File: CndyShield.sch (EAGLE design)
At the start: 19 parts, among them U1 ARDUINOR3-BPLACE

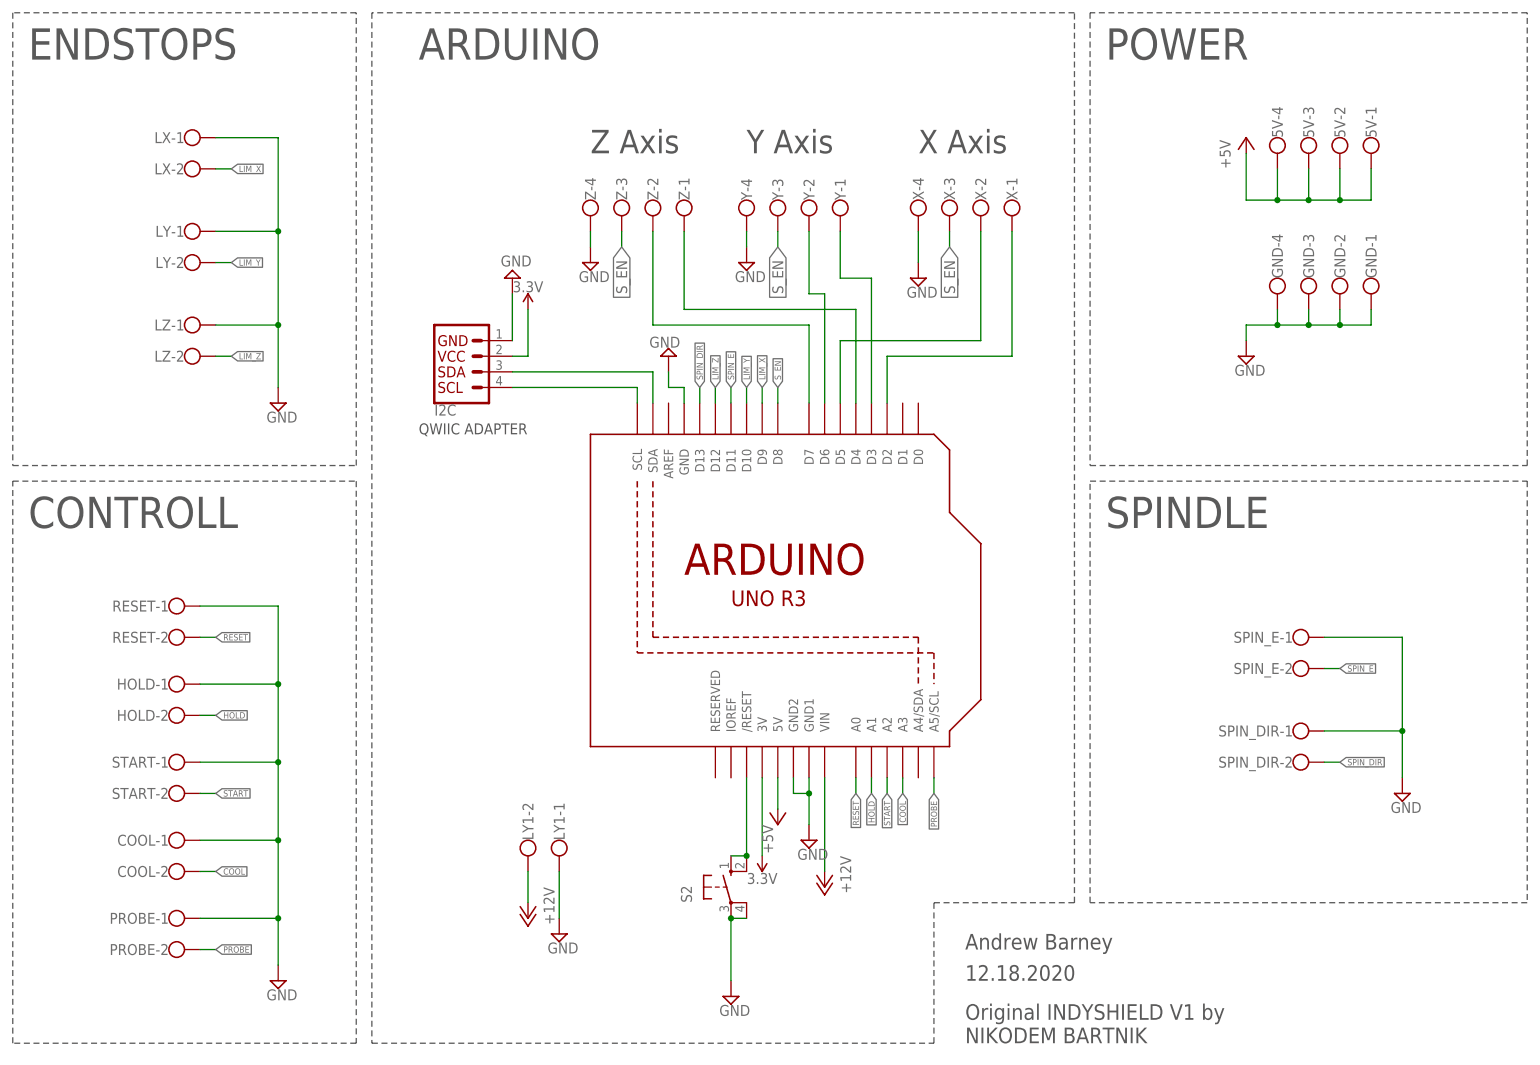
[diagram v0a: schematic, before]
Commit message: Add files via upload
V1.1 : remapped analog breakouts. Added filter capacitors. Added Alarm State LED on A4.
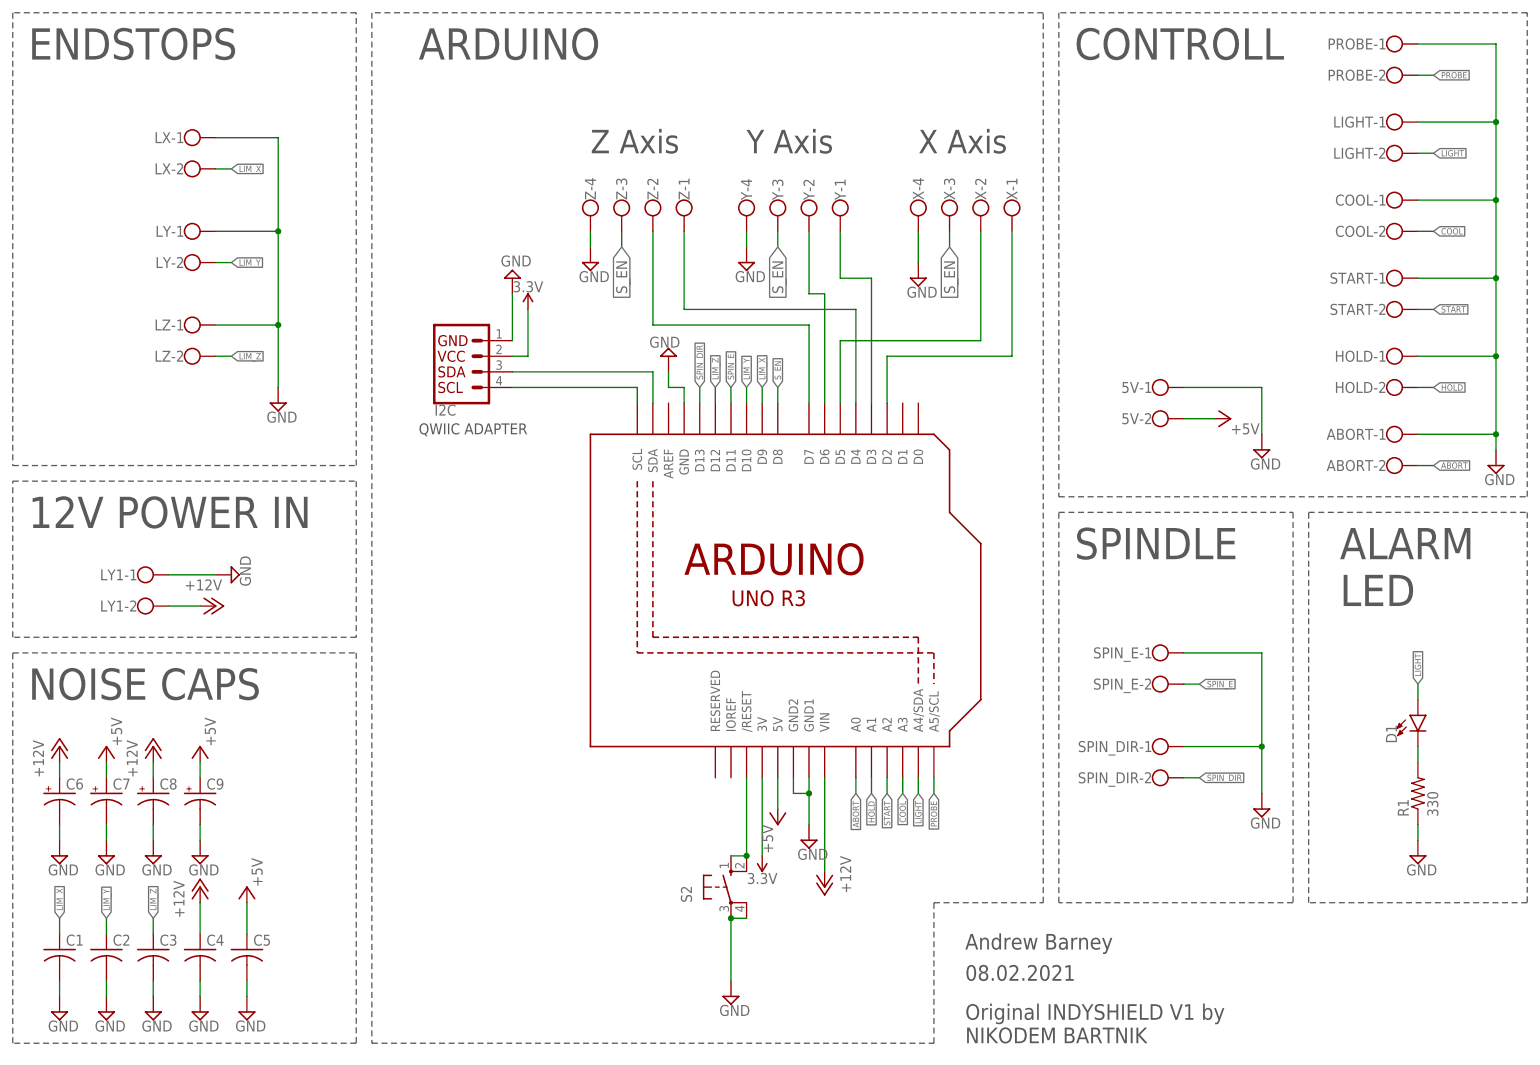
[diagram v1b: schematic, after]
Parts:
- removed GND: (no value), con-wago-500:W237-4
- removed RESET: (no value), con-wago-500:W237-102
- added ABORT, LIGHT: (no value), con-wago-500:W237-102
- added C1, C2, C3, C4, C5: (no value), adafruit:C-US025-024X044
- added C6, C7, C8, C9: (no value), adafruit:CPOL-USE1.8-4
- added D1: (no value), SparkFun-LED:LED5MM
- added R1: 330, adafruit:R-US_0207/10
- 5V: device con-wago-500:W237-4 -> con-wago-500:W237-102
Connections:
- removed net RESET: RESET-2.KL, U1.A0
- new net ABORT: ABORT-2.KL, U1.A0
- new net LIGHT: D1.A, LIGHT-2.KL, U1.A4/SDA
- new net N$8: D1.C, R1.2
- net +12V: now also C4.1, C6.+, C8.+
- net +5V: now also C5.1, C7.+, C9.+; no longer 5V-1.KL, 5V-3.KL, 5V-4.KL
- net GND: now also 5V-1.KL, ABORT-1.KL, C1.2, C2.2, C3.2, C4.2, C5.2, C6.-, C7.-, C8.-, C9.-, LIGHT-1.KL, R1.1; no longer GND-1.KL, GND-2.KL, GND-3.KL, GND-4.KL, RESET-1.KL
- net LIM_X: now also C1.1
- net LIM_Y: now also C2.1
- net LIM_Z: now also C3.1
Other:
- note added: "08.02.2021"
- note added: "12V POWER IN"
- note added: "ALARM LED"
- note added: "NOISE CAPS"
- note removed: "12.18.2020"
- note removed: "POWER"
- moved on the sheet: 5V-1, 5V-2, COOL-1, COOL-2, HOLD-1, HOLD-2, LY1-1, LY1-2, PROBE-1, PROBE-2, SPIN_DIR-1, SPIN_DIR-2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

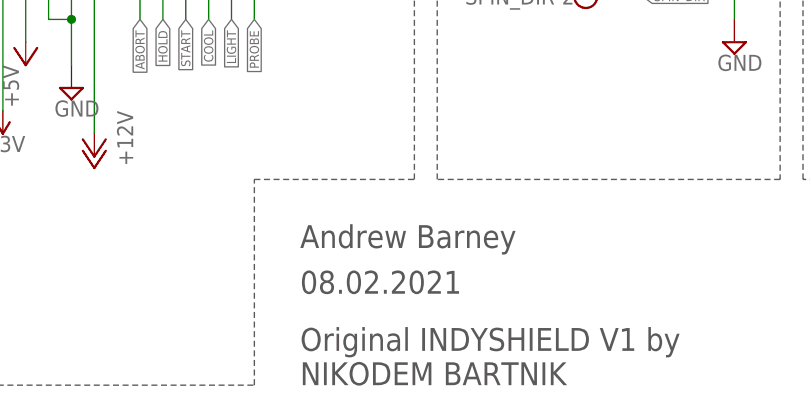
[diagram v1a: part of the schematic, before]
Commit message: Add files via upload
minor silkscreen change for Analog 4. Changed LIGHT to MIST to be more consistent with official GRBL port use.
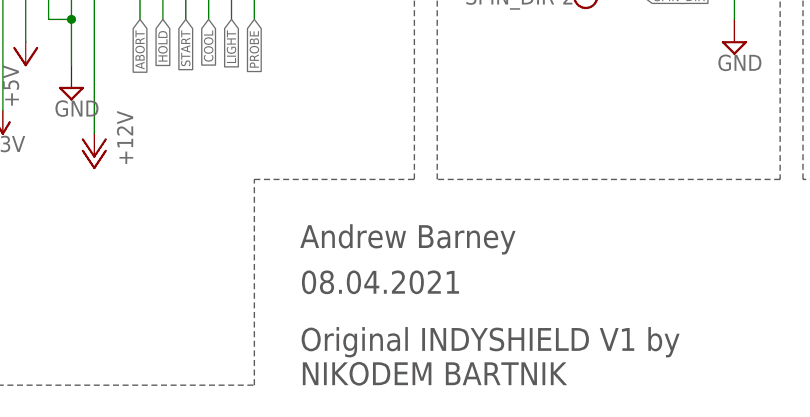
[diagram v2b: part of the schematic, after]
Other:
- note added: "08.04.2021"
- note removed: "08.02.2021"
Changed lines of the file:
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@@
 <text x="10.16" y="88.9" size="5.08" layer="97">12V POWER IN</text>
 <text x="162.56" y="20.32" size="2.54" layer="97">Andrew Barney</text>
-<text x="162.56" y="15.24" size="2.54" layer="97">08.02.2021</text>
+<text x="162.56" y="15.24" size="2.54" layer="97">08.04.2021</text>
 <text x="73.66" y="104.14" size="1.778" layer="97">QWIIC ADAPTER</text>
 <text x="162.56" y="5.08" size="2.54" layer="97">Original INDYSHIELD V1 by

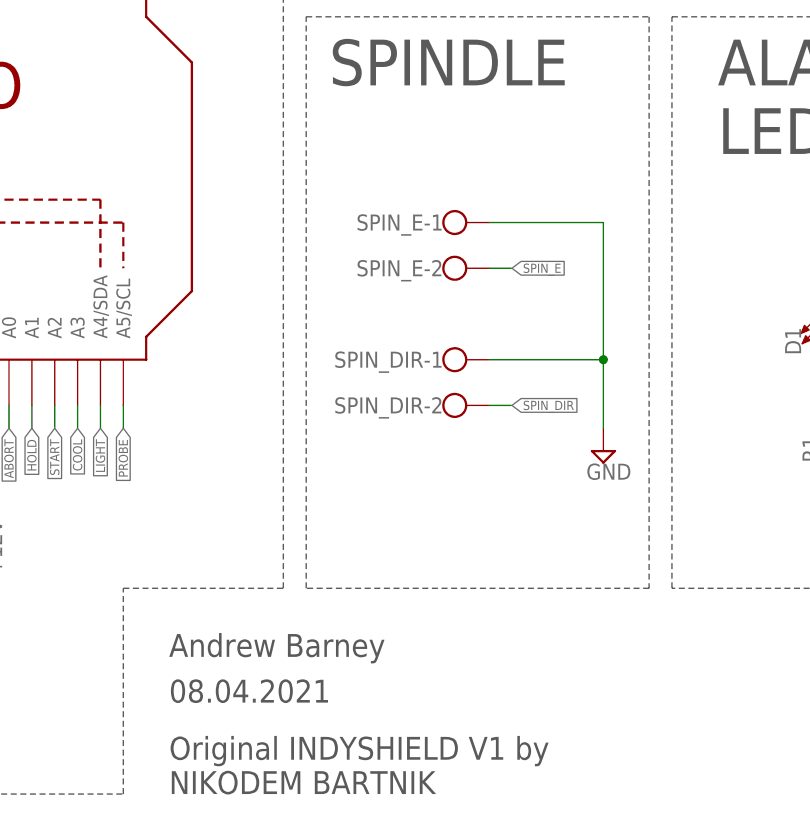
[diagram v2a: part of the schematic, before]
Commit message: Add files via upload
V1.2: Fixed swapped silkscreen text for Spindle PWM and Spindle Direction. Added optional LED to Spindle PWM (pin 11) as an optional safety warning light.
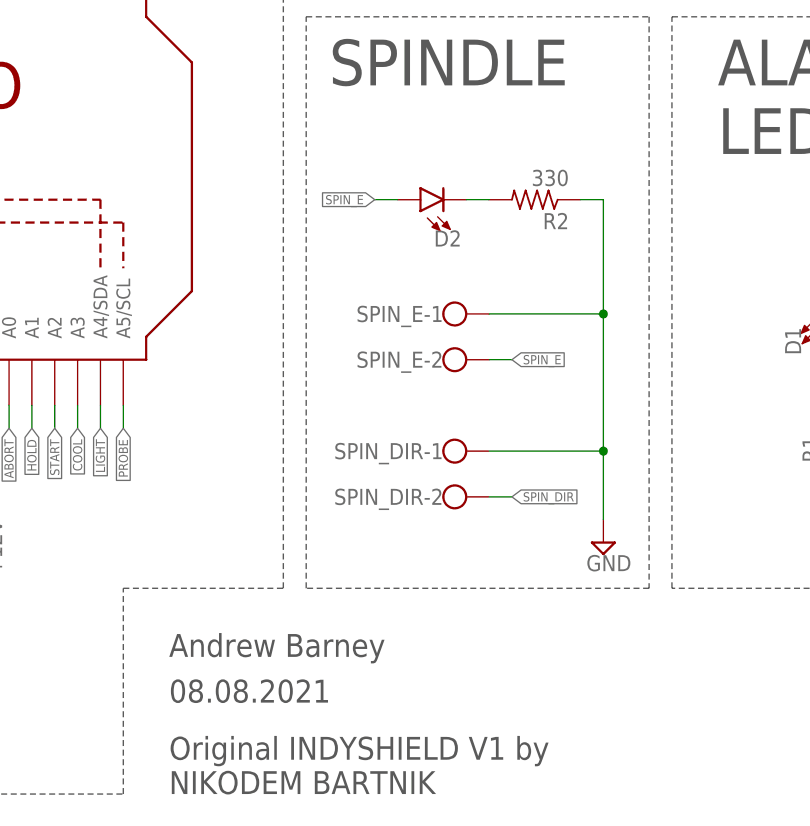
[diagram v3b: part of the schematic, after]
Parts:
- added D2: (no value), SparkFun-LED:LED5MM
- added R2: 330, adafruit:R-US_0207/10
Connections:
- new net N$11: D2.C, R2.2
- net GND: now also R2.1
- net SPIN_E: now also D2.A
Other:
- note added: "08.08.2021"
- note removed: "08.04.2021"
- moved on the sheet: SPIN_DIR-1, SPIN_DIR-2, SPIN_E-1, SPIN_E-2
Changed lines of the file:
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@@
 <part name="P+9" library="supply1" library_urn="urn:adsk.eagle:library:371" deviceset="+12V" device=""/>
 <part name="P+10" library="supply1" library_urn="urn:adsk.eagle:library:371" deviceset="+5V" device=""/>
+<part name="D2" library="SparkFun-LED" library_urn="urn:adsk.eagle:library:529" deviceset="LED" device="5MM" package3d_urn="urn:adsk.eagle:package:39353/1"/>
+<part name="R2" library="adafruit" library_urn="urn:adsk.eagle:library:420" deviceset="R-US_" device="0207/10" package3d_urn="urn:adsk.eagle:package:6240597/1" value="330"/>
 </parts>
 <sheets>
@@
 <text x="10.16" y="88.9" size="5.08" layer="97">12V POWER IN</text>
 <text x="162.56" y="20.32" size="2.54" layer="97">Andrew Barney</text>
-<text x="162.56" y="15.24" size="2.54" layer="97">08.04.2021</text>
+<text x="162.56" y="15.24" size="2.54" layer="97">08.08.2021</text>
 <text x="73.66" y="104.14" size="1.778" layer="97">QWIIC ADAPTER</text>
 <text x="162.56" y="5.08" size="2.54" layer="97">Original INDYSHIELD V1 by
@@
 <attribute name="VALUE" x="48.895" y="106.045" size="1.778" layer="96"/>
 </instance>
-<instance part="SPIN_E" gate="-1" x="193.04" y="68.58" smashed="yes">
-<attribute name="NAME" x="193.04" y="69.469" size="1.778" layer="95" rot="R180"/>
-</instance>
-<instance part="SPIN_E" gate="-2" x="193.04" y="63.5" smashed="yes">
-<attribute name="VALUE" x="190.5" y="59.817" size="1.778" layer="96"/>
-<attribute name="NAME" x="193.04" y="64.389" size="1.778" layer="95" rot="R180"/>
-</instance>
-<instance part="SPIN_DIR" gate="-1" x="193.04" y="53.34" smashed="yes">
+<instance part="SPIN_E" gate="-1" x="193.04" y="58.42" smashed="yes">
+<attribute name="NAME" x="193.04" y="59.309" size="1.778" layer="95" rot="R180"/>
+</instance>
+<instance part="SPIN_E" gate="-2" x="193.04" y="53.34" smashed="yes">
+<attribute name="VALUE" x="190.5" y="49.657" size="1.778" layer="96"/>
 <attribute name="NAME" x="193.04" y="54.229" size="1.778" layer="95" rot="R180"/>
 </instance>
-<instance part="SPIN_DIR" gate="-2" x="193.04" y="48.26" smashed="yes">
-<attribute name="VALUE" x="190.5" y="44.577" size="1.778" layer="96"/>
-<attribute name="NAME" x="193.04" y="49.149" size="1.778" layer="95" rot="R180"/>
-</instance>
-<instance part="SUPPLY6" gate="GND" x="210.82" y="43.18" smashed="yes">
-<attribute name="VALUE" x="208.915" y="40.005" size="1.778" layer="96"/>
+<instance part="SPIN_DIR" gate="-1" x="193.04" y="43.18" smashed="yes">
+<attribute name="NAME" x="193.04" y="44.069" size="1.778" layer="95" rot="R180"/>
+</instance>
+<instance part="SPIN_DIR" gate="-2" x="193.04" y="38.1" smashed="yes">
+<attribute name="VALUE" x="190.5" y="34.417" size="1.778" layer="96"/>
+<attribute name="NAME" x="193.04" y="38.989" size="1.778" layer="95" rot="R180"/>
+</instance>
+<instance part="SUPPLY6" gate="GND" x="210.82" y="33.02" smashed="yes">
+<attribute name="VALUE" x="208.915" y="29.845" size="1.778" layer="96"/>
 </instance>
 <instance part="SUPPLY7" gate="GND" x="114.3" y="116.84" smashed="yes" rot="R180">
@@
 <instance part="P+10" gate="1" x="38.1" y="53.34" smashed="yes">
 <attribute name="VALUE" x="40.64" y="53.34" size="1.778" layer="96" rot="R90"/>
+</instance>
+<instance part="D2" gate="G$1" x="190.5" y="71.12" smashed="yes" rot="R90">
+<attribute name="NAME" x="195.072" y="67.691" size="1.778" layer="95" font="vector" rot="R180"/>
+<attribute name="VALUE" x="195.072" y="73.025" size="1.778" layer="96" font="vector" rot="R180" align="top-left"/>
+</instance>
+<instance part="R2" gate="G$1" x="203.2" y="71.12" smashed="yes" rot="R180">
+<attribute name="NAME" x="207.01" y="69.6214" size="1.778" layer="95" rot="R180"/>
+<attribute name="VALUE" x="207.01" y="74.422" size="1.778" layer="96" rot="R180"/>
 </instance>
 </instances>
@@
 <pinref part="SPIN_E" gate="-1" pin="KL"/>
 <pinref part="SUPPLY6" gate="GND" pin="GND"/>
-<wire x1="198.12" y1="68.58" x2="210.82" y2="68.58" width="0.1524" layer="91"/>
-<wire x1="210.82" y1="68.58" x2="210.82" y2="53.34" width="0.1524" layer="91"/>
+<wire x1="198.12" y1="58.42" x2="210.82" y2="58.42" width="0.1524" layer="91"/>
+<wire x1="210.82" y1="58.42" x2="210.82" y2="43.18" width="0.1524" layer="91"/>
 <pinref part="SPIN_DIR" gate="-1" pin="KL"/>
-<wire x1="210.82" y1="53.34" x2="210.82" y2="45.72" width="0.1524" layer="91"/>
-<wire x1="198.12" y1="53.34" x2="210.82" y2="53.34" width="0.1524" layer="91"/>
-<junction x="210.82" y="53.34"/>
+<wire x1="210.82" y1="43.18" x2="210.82" y2="35.56" width="0.1524" layer="91"/>
+<wire x1="198.12" y1="43.18" x2="210.82" y2="43.18" width="0.1524" layer="91"/>
+<junction x="210.82" y="43.18"/>
+<pinref part="R2" gate="G$1" pin="1"/>
+<wire x1="208.28" y1="71.12" x2="210.82" y2="71.12" width="0.1524" layer="91"/>
+<wire x1="210.82" y1="71.12" x2="210.82" y2="58.42" width="0.1524" layer="91"/>
+<junction x="210.82" y="58.42"/>
 </segment>
 <segment>
@@
 <segment>
 <pinref part="SPIN_E" gate="-2" pin="KL"/>
-<wire x1="198.12" y1="63.5" x2="200.66" y2="63.5" width="0.1524" layer="91"/>
-<label x="200.66" y="63.5" size="1.016" layer="95" xref="yes"/>
+<wire x1="198.12" y1="53.34" x2="200.66" y2="53.34" width="0.1524" layer="91"/>
+<label x="200.66" y="53.34" size="1.016" layer="95" xref="yes"/>
+<label x="185.42" y="71.12" size="1.016" layer="95" rot="R180" xref="yes"/>
 </segment>
 <segment>
@@
 <label x="124.46" y="111.76" size="1.016" layer="95" rot="R90" xref="yes"/>
 </segment>
+<segment>
+<wire x1="185.42" y1="71.12" x2="187.96" y2="71.12" width="0.1524" layer="91"/>
+<pinref part="D2" gate="G$1" pin="A"/>
+</segment>
 </net>
 <net name="SPIN_DIR" class="0">
@@
 <segment>
 <pinref part="SPIN_DIR" gate="-2" pin="KL"/>
-<wire x1="198.12" y1="48.26" x2="200.66" y2="48.26" width="0.1524" layer="91"/>
-<label x="200.66" y="48.26" size="1.016" layer="95" xref="yes"/>
+<wire x1="198.12" y1="38.1" x2="200.66" y2="38.1" width="0.1524" layer="91"/>
+<label x="200.66" y="38.1" size="1.016" layer="95" xref="yes"/>
 </segment>
 </net>
@@
 </segment>
 </net>
+<net name="N$11" class="0">
+<segment>
+<pinref part="D2" gate="G$1" pin="C"/>
+<pinref part="R2" gate="G$1" pin="2"/>
+<wire x1="195.58" y1="71.12" x2="198.12" y2="71.12" width="0.1524" layer="91"/>
+</segment>
+</net>

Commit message: Add files via upload
V1.3 Updated Silkscreen. Added OSHW Logo. Noise reduction caps.
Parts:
- added C10, C11, C12, C13: (no value), adafruit:C-US025-024X044
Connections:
- new net MIST: D1.A, U1.A4/SDA
- net ABORT: now also C10.1
- net GND: now also C10.2, C11.2, C12.2, C13.2
- net HOLD: now also C11.1
- net LIGHT: no longer D1.A, U1.A4/SDA
- net PROBE: now also C13.1
- net START: now also C12.1
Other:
- moved on the sheet: C4, C5

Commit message: Add files via upload
CN0DY Shield for GRBL V1.2. Ready for production. Fixed swapped silkscreen with spindle direction and spindle PWM. Added a number of new optional components. Added OSHW logo.
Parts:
- removed C11, C12, C13: (no value), adafruit:C-US025-024X044
- added LOGO1: OSHW-LOGOM, RMR:OSHW-LOGOM
- added RESET: (no value), con-wago-500:W237-102
- C10: device adafruit:C-US025-024X044 -> adafruit:CPOL-USE1.8-4
- C6, C7, C8: device adafruit:CPOL-USE1.8-4 -> adafruit:C-US025-024X044
- R1, R2: value 330 -> 150
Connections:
- removed net N$7: S2.S, S2.S1, U1./RESET
- new net RESET: RESET-2.KL, S2.S, S2.S1, U1./RESET
- net +12V: now also C10.+, C8.1, C9.+; no longer C4.1, C6.+, C8.+
- net +5V: no longer C5.1, C7.+, C9.+
- net ABORT: now also C4.1; no longer C10.1
- net GND: now also C10.-, C6.2, C7.2, C8.2, RESET-1.KL; no longer C10.2, C11.2, C12.2, C13.2, C6.-, C7.-, C8.-
- net HOLD: now also C5.1; no longer C11.1
- net PROBE: now also C7.1; no longer C13.1
- net START: now also C6.1; no longer C12.1
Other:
- note added: "Rabbit Mountain Research Andrew Barney 08.08.2021"
- note removed: "08.08.2021"
- note removed: "Andrew Barney"
- moved on the sheet: C1, C2, C3, C4, C5, C9, LX-1, LX-2, LY-1, LY-2, LY1-1, LY1-2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
